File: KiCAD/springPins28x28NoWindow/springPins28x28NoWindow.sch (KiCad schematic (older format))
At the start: 23 parts, among them J1 CONN_02X06, J2 CONN_02X06

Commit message: new 28x28 spring pin board done
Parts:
- R1: renamed from 100k1; value R -> 100k
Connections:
- net labels added: BOT_CU, GND, GNDA, TOP_CU
- wire segments 6 -> 10
- no-connect marks 2 -> 0
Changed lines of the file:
@@
 LIBS:contrib
 LIBS:valves
+LIBS:springPins28x28NoWindow-cache
 EELAYER 25 0
 EELAYER END
@@
 F 3 "" H 4600 2700 50  0001 C CNN
 	1    4600 3900
-	1    0    0    -1
+	1    0    0    1
 $EndComp
 $Comp
@@
 F 3 "" H 5750 2700 50  0001 C CNN
 	1    5750 3900
-	1    0    0    -1
+	1    0    0    1
 $EndComp
 Text GLabel 4350 3650 0    60   Input ~ 0
@@
 2_I
 $Comp
-L R 100k1
+L R R1
 U 1 1 599DBDE1
 P 4600 4500
-F 0 "100k1" V 4680 4500 50  0000 C CNN
-F 1 "R" V 4600 4500 50  0000 C CNN
+F 0 "R1" V 4680 4500 50  0000 C CNN
+F 1 "100k" V 4600 4500 50  0000 C CNN
 F 2 "Resistors_SMD:R_0805_HandSoldering" V 4530 4500 50  0001 C CNN
 F 3 "" H 4600 4500 50  0001 C CNN
@@
 Text GLabel 5500 4050 0    60   Input ~ 0
 1_V
-NoConn ~ 6000 3650
-NoConn ~ 5500 3650
+Text GLabel 6000 3650 2    60   Input ~ 0
+TOP_CU
+Text GLabel 5500 3650 0    60   Input ~ 0
+BOT_CU
+$Comp
+L GND #PWR01
+U 1 1 599DC5F7
+P 8450 2600
+F 0 "#PWR01" H 8450 2350 50  0001 C CNN
+F 1 "GND" H 8450 2450 50  0000 C CNN
+F 2 "" H 8450 2600 50  0001 C CNN
+F 3 "" H 8450 2600 50  0001 C CNN
+	1    8450 2600
+	1    0    0    -1
+$EndComp
+$Comp
+L GNDA #PWR02
+U 1 1 599DCCE9
+P 8750 2600
+F 0 "#PWR02" H 8750 2350 50  0001 C CNN
+F 1 "GNDA" H 8750 2450 50  0000 C CNN
+F 2 "" H 8750 2600 50  0001 C CNN
+F 3 "" H 8750 2600 50  0001 C CNN
+	1    8750 2600
+	1    0    0    -1
+$EndComp
+Text GLabel 8750 2500 1    60   Input ~ 0
+BOT_CU
+Text GLabel 8450 2500 1    60   Input ~ 0
+TOP_CU
+$Comp
+L PWR_FLAG #FLG03
+U 1 1 599DD196
+P 8950 2550
+F 0 "#FLG03" H 8950 2625 50  0001 C CNN
+F 1 "PWR_FLAG" H 8950 2700 50  0000 C CNN
+F 2 "" H 8950 2550 50  0001 C CNN
+F 3 "" H 8950 2550 50  0001 C CNN
+	1    8950 2550
+	0    1    1    0
+$EndComp
+$Comp
+L PWR_FLAG #FLG04
+U 1 1 599DD1ED
+P 8250 2550
+F 0 "#FLG04" H 8250 2625 50  0001 C CNN
+F 1 "PWR_FLAG" H 8250 2700 50  0000 C CNN
+F 2 "" H 8250 2550 50  0001 C CNN
+F 3 "" H 8250 2550 50  0001 C CNN
+	1    8250 2550
+	0    -1   -1   0
+$EndComp
+Wire Wire Line
+	8450 2500 8450 2600
+Wire Wire Line
+	8250 2550 8450 2550
+Connection ~ 8450 2550
+Wire Wire Line
+	8950 2550 8750 2550
+Wire Wire Line
+	8750 2500 8750 2600
+Connection ~ 8750 2550
 $EndSCHEMATC

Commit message: nowindow pin boards done
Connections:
- net labels added: BCu, FCu, I1, I2, I3, I4, I5, I6, I7, I8, IB, IT, RH, RL, V1, V2, V3, V4, V5, V6, V7, V8, VB, VT
- net labels removed: 1_I, 1_V, 2_I, 2_V, 3_I, 3_V, 4_I, 4_V, 5_I, 5_V, 6_I, 6_V, 7_I, 7_V, 8_I, 8_V, BOT_CU, B_I, B_V, GND, GNDA, TOP_CU, T_I, T_V
- wire segments 10 -> 60
- no-connect marks 0 -> 2
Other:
- note added: "+"
- note removed: "x"
- moved on the sheet: R1

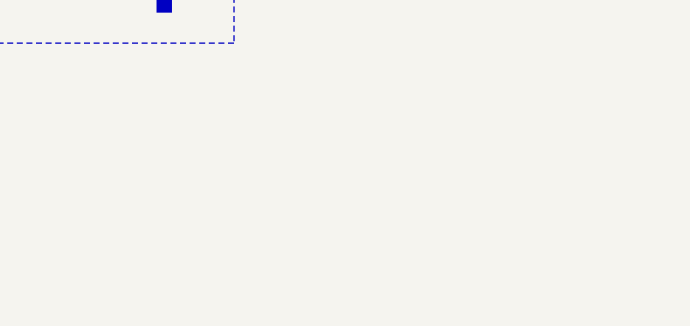
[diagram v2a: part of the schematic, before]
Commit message: spruce up 28x28NoWindow
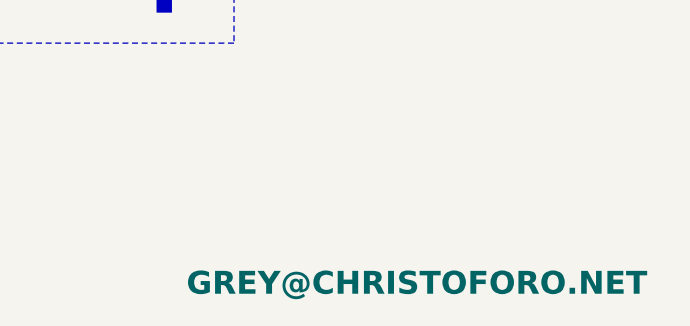
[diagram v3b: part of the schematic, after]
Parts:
- added L1: GREY@CHRISTOFORO.NET, myParts:logo_small, symbol GREY@CHRISTOFORO.NET
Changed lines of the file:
@@
 LIBS:contrib
 LIBS:valves
+LIBS:myParts
 LIBS:springPins28x28NoWindow-cache
 EELAYER 25 0
@@
 Text Label 5350 4050 0    60   ~ 0
 BCu
+$Comp
+L GREY@CHRISTOFORO.NET L1
+U 1 1 59BFAA22
+P 8000 7000
+F 0 "L1" H 8000 6875 60  0001 C CNN
+F 1 "GREY@CHRISTOFORO.NET" H 8000 7000 100 0000 C CNB
+F 2 "myParts:logo_small" H 8000 7000 60  0001 C CNN
+F 3 "" H 8000 7000 60  0001 C CNN
+	1    8000 7000
+	1    0    0    -1
+$EndComp
 $EndSCHEMATC

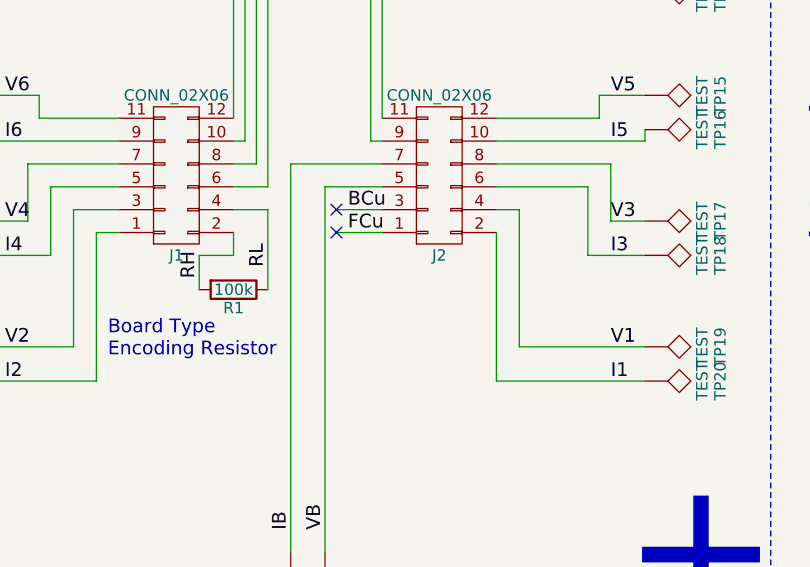
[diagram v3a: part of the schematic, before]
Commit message: make spring pin board pin holders smaller, update base1x, update mux design controller board
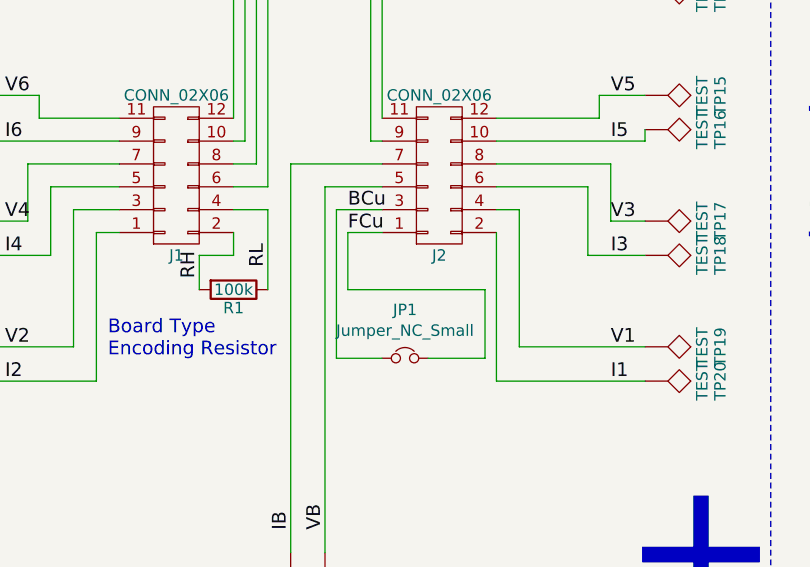
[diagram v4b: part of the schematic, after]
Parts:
- added JP1: Jumper_NC_Small, Connectors:GS2, symbol Jumper_NC_Small
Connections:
- net BCu: now also JP1.1
- net FCu: now also JP1.2
- no-connect marks 2 -> 0
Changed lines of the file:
@@
 LIBS:myParts
 LIBS:springPins28x28NoWindow-cache
-EELAYER 25 0
+EELAYER 26 0
 EELAYER END
 $Descr A4 11693 8268
@@
 RH
 Wire Wire Line
-	5300 4150 5500 4150
-Wire Wire Line
 	5500 4050 5300 4050
-NoConn ~ 5300 4150
-NoConn ~ 5300 4050
 Text Label 5350 4150 0    60   ~ 0
 FCu
@@
 	1    0    0    -1
 $EndComp
+$Comp
+L Jumper_NC_Small JP1
+U 1 1 59F642BD
+P 5600 4700
+F 0 "JP1" H 5600 4912 50  0000 C CNN
+F 1 "Jumper_NC_Small" H 5600 4821 50  0000 C CNN
+F 2 "Connectors:GS2" H 5600 4700 50  0001 C CNN
+F 3 "" H 5600 4700 50  0001 C CNN
+	1    5600 4700
+	1    0    0    -1
+$EndComp
+Wire Wire Line
+	5500 4150 5350 4150
+Wire Wire Line
+	5350 4150 5350 4400
+Wire Wire Line
+	5350 4400 5950 4400
+Wire Wire Line
+	5950 4400 5950 4700
+Wire Wire Line
+	5950 4700 5700 4700
+Wire Wire Line
+	5500 4700 5300 4700
+Wire Wire Line
+	5300 4700 5300 4050
 $EndSCHEMATC

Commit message: spruce up spring pin boards
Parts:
- J1, J2: symbol CONN_02X06 -> Connector:Conn_02x06_Odd_Even
- JP1: symbol Jumper_NC_Small -> device:Jumper_NC_Small
- L1: symbol GREY@CHRISTOFORO.NET -> myParts:GREY@CHRISTOFORO.NET
- R1: symbol R -> device:R
- TP1, TP10, TP11, TP12, TP13, TP14, TP15, TP16, TP17, TP18, TP19, TP2, TP20, TP3, TP4, TP5, TP6, TP7, TP8, TP9: symbol TEST -> Connector:Test_Point
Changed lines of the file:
@@
-EESchema Schematic File Version 2
-LIBS:power
-LIBS:device
-LIBS:transistors
-LIBS:conn
-LIBS:linear
-LIBS:regul
-LIBS:74xx
-LIBS:cmos4000
-LIBS:adc-dac
-LIBS:memory
-LIBS:xilinx
-LIBS:microcontrollers
-LIBS:dsp
-LIBS:microchip
-LIBS:analog_switches
-LIBS:motorola
-LIBS:texas
-LIBS:intel
-LIBS:audio
-LIBS:interface
-LIBS:digital-audio
-LIBS:philips
-LIBS:display
-LIBS:cypress
-LIBS:siliconi
-LIBS:opto
-LIBS:atmel
-LIBS:contrib
-LIBS:valves
-LIBS:myParts
+EESchema Schematic File Version 4
 LIBS:springPins28x28NoWindow-cache
 EELAYER 26 0
@@
 $EndDescr
 $Comp
-L TEST TP10
+L Connector:Test_Point TP10
 U 1 1 58E4C4C8
 P 5100 5550
@@
 $EndComp
 $Comp
-L TEST TP6
+L Connector:Test_Point TP6
 U 1 1 58E4C4F2
 P 3750 4250
@@
 $EndComp
 $Comp
-L TEST TP5
+L Connector:Test_Point TP5
 U 1 1 58E4C553
 P 3750 4100
@@
 $EndComp
 $Comp
-L TEST TP8
+L Connector:Test_Point TP8
 U 1 1 58E4C6B7
 P 3750 4800
@@
 $EndComp
 $Comp
-L TEST TP7
+L Connector:Test_Point TP7
 U 1 1 58E4C6BD
 P 3750 4650
@@
 $EndComp
 $Comp
-L TEST TP4
+L Connector:Test_Point TP4
 U 1 1 58E4C747
 P 3750 3700
@@
 $EndComp
 $Comp
-L TEST TP3
+L Connector:Test_Point TP3
 U 1 1 58E4C74D
 P 3750 3550
@@
 $EndComp
 $Comp
-L TEST TP18
+L Connector:Test_Point TP18
 U 1 1 58E4CA5F
 P 6650 4250
@@
 $EndComp
 $Comp
-L TEST TP17
+L Connector:Test_Point TP17
 U 1 1 58E4CA65
 P 6650 4100
@@
 $EndComp
 $Comp
-L TEST TP20
+L Connector:Test_Point TP20
 U 1 1 58E4CA6B
 P 6650 4800
@@
 $EndComp
 $Comp
-L TEST TP19
+L Connector:Test_Point TP19
 U 1 1 58E4CA71
 P 6650 4650
@@
 $EndComp
 $Comp
-L TEST TP16
+L Connector:Test_Point TP16
 U 1 1 58E4CA77
 P 6650 3700
@@
 $EndComp
 $Comp
-L TEST TP15
+L Connector:Test_Point TP15
 U 1 1 58E4CA7D
 P 6650 3550
@@
 $EndComp
 $Comp
-L TEST TP9
+L Connector:Test_Point TP9
 U 1 1 58E4CC43
 P 4950 2300
@@
 $EndComp
 $Comp
-L TEST TP11
+L Connector:Test_Point TP11
 U 1 1 58E4CC49
 P 5150 2300
@@
 o
 $Comp
-L TEST TP2
+L Connector:Test_Point TP2
 U 1 1 599D95E4
 P 3700 3100
@@
 $EndComp
 $Comp
-L TEST TP1
+L Connector:Test_Point TP1
 U 1 1 599D95EA
 P 3700 2950
@@
 $EndComp
 $Comp
-L TEST TP14
+L Connector:Test_Point TP14
 U 1 1 599D9D84
 P 6650 3100
@@
 $EndComp
 $Comp
-L TEST TP13
+L Connector:Test_Point TP13
 U 1 1 599D9D8A
 P 6650 2950
@@
 8
 $Comp
-L CONN_02X06 J1
+L Connector:Conn_02x06_Odd_Even J1
 U 1 1 599DB107
-P 4600 3900
-F 0 "J1" H 4600 4250 50  0000 C CNN
-F 1 "CONN_02X06" H 4600 3550 50  0000 C CNN
-F 2 "Pin_Headers:Pin_Header_Straight_2x06_Pitch2.54mm" H 4600 2700 50  0001 C CNN
-F 3 "" H 4600 2700 50  0001 C CNN
-	1    4600 3900
+P 4550 3950
+F 0 "J1" H 4450 4250 50  0000 C CNN
+F 1 "CONN_02X06" H 4550 3500 50  0000 C CNN
+F 2 "Pin_Headers:Pin_Header_Straight_2x06_Pitch2.54mm" H 4550 2750 50  0001 C CNN
+F 3 "" H 4550 2750 50  0001 C CNN
+	1    4550 3950
 	1    0    0    1
 $EndComp
 $Comp
-L CONN_02X06 J2
+L Connector:Conn_02x06_Odd_Even J2
 U 1 1 599DB1BB
-P 5750 3900
-F 0 "J2" H 5750 4250 50  0000 C CNN
-F 1 "CONN_02X06" H 5750 3550 50  0000 C CNN
-F 2 "Pin_Headers:Pin_Header_Straight_2x06_Pitch2.54mm" H 5750 2700 50  0001 C CNN
-F 3 "" H 5750 2700 50  0001 C CNN
-	1    5750 3900
+P 5700 3950
+F 0 "J2" H 5600 4250 50  0000 C CNN
+F 1 "CONN_02X06" H 5750 3500 50  0000 C CNN
+F 2 "Pin_Headers:Pin_Header_Straight_2x06_Pitch2.54mm" H 5700 2750 50  0001 C CNN
+F 3 "" H 5700 2750 50  0001 C CNN
+	1    5700 3950
 	1    0    0    1
 $EndComp
 $Comp
-L R R1
+L device:R R1
 U 1 1 599DBDE1
 P 4850 4400
@@
 	5450 3750 5500 3750
 $Comp
-L TEST TP12
+L Connector:Test_Point TP12
 U 1 1 58E4C3ED
 P 5250 5550
@@
 BCu
 $Comp
-L GREY@CHRISTOFORO.NET L1
+L myParts:GREY@CHRISTOFORO.NET L1
 U 1 1 59BFAA22
 P 8000 7000
@@
 $EndComp
 $Comp
-L Jumper_NC_Small JP1
+L device:Jumper_NC_Small JP1
 U 1 1 59F642BD
 P 5600 4700
